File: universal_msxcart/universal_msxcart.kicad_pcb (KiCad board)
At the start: 2 copper layers, 102.5 x 65 mm, 9 parts, among them J1 Conn_01x21_Pin, P1 CONN_02X25, U1 74HC244, U2 74HC244, U3 74HC244, U4 TXB0108PW, U5 74LS08, U6 74LS05, U7 74LS139

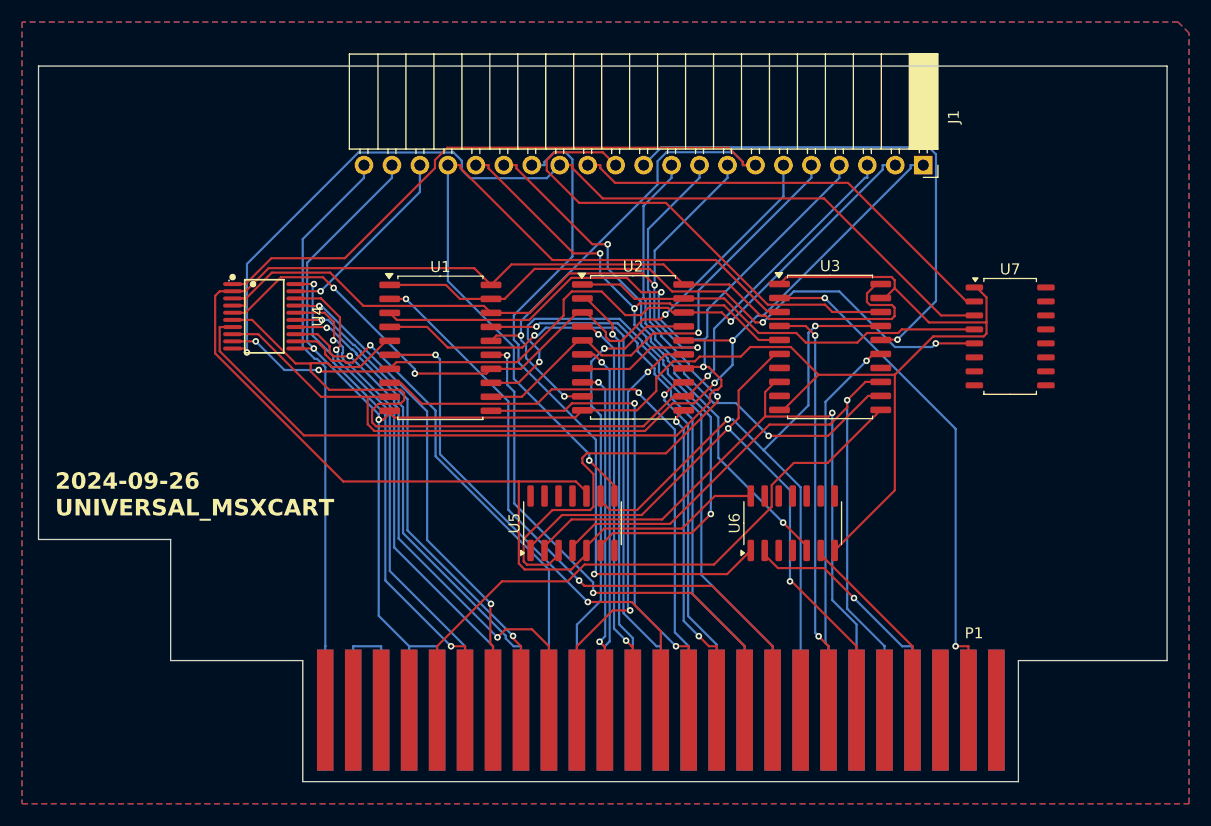
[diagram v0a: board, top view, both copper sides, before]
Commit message: epm240_msxcart/epm240_msxcart.kicad_pcb epm240_msxcart/epm240_msxcart.kicad_prl epm240_msxcart/epm240_msxcart.kicad_sch epm240_msxcart/fp-info-cache epm240_msxcart/freerouting.dsn epm240_msxcart/freerouting.ses universal_msxcart/.gitignore universal_msxcart/fp-info-cache universal_msxcart/universal_msxcart.kicad_pcb universal_msxcart/universal_msxcart.kicad_prl universal_msxcart/universal_msxcart.kicad_sch
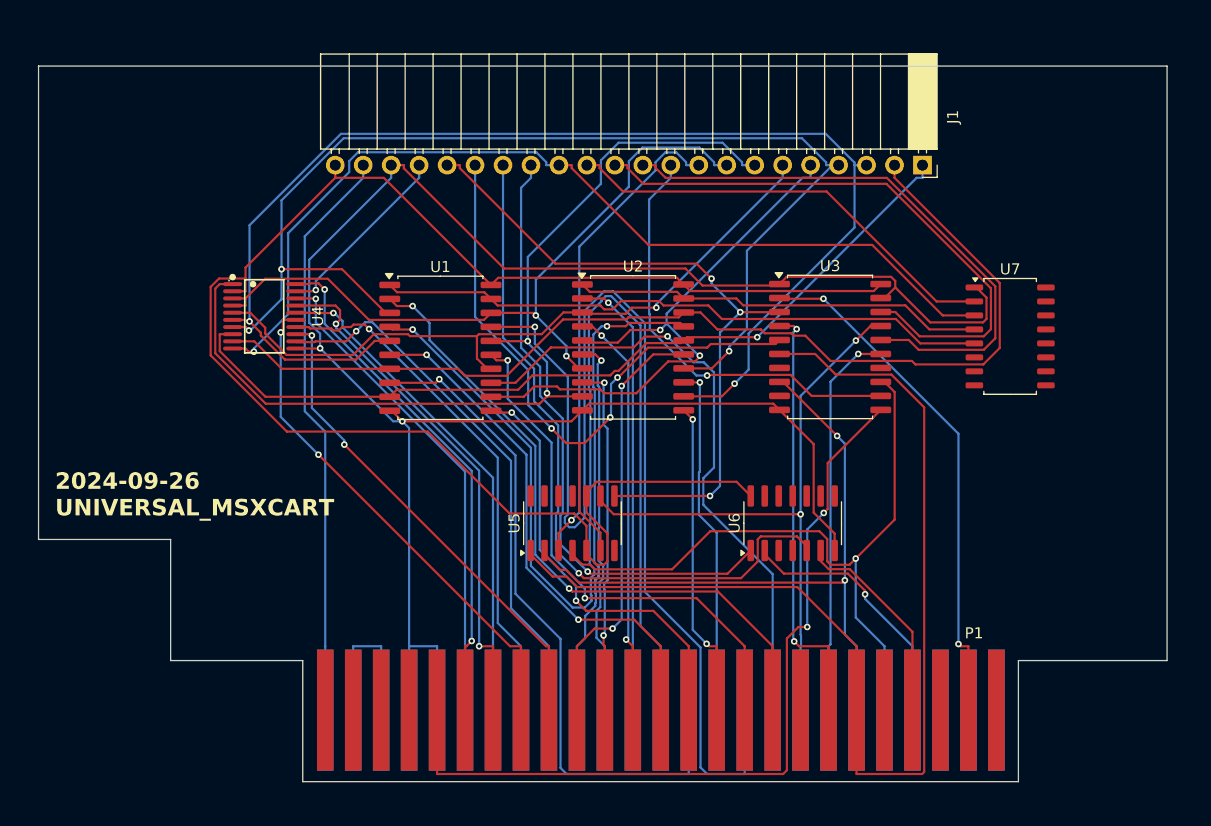
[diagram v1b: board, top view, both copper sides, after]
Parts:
- J1: footprint Connector_PinSocket_2.54mm:PinSocket_1x21_P2.54mm_Horizontal -> Connector_PinSocket_2.54mm:PinSocket_1x22_P2.54mm_Horizontal
- moved J1 0.07 mm to (158.8, 57.0)
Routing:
- net /A11: track 51.6 -> 104.1 mm
- net /A14: track 58.7 -> 104.1 mm
- net /MREQ: track 62.2 -> 99.5 mm, vias 2 -> 0
- net /RD2: track 89.9 -> 115.6 mm, vias 1 -> 2
- net /RD1: track 73.0 -> 96.5 mm, vias 3 -> 0
- net /CLK: track 56.2 -> 74.4 mm, vias 0 -> 2
- net /RC15: track 47.9 -> 64.5 mm, vias 2 -> 1
- net /RC8: track 58.9 -> 43.8 mm
- net /RD4: track 41.9 -> 54.0 mm, vias 1 -> 2
- net /RD7: track 77.6 -> 66.5 mm
- net /RD3: track 116.8 -> 105.9 mm, vias 2 -> 3
- net /RC11: track 43.6 -> 53.9 mm
- net /RC17: track 72.1 -> 62.7 mm, vias 1 -> 3
- net /RD6: track 96.5 -> 87.0 mm
- net /RD0: track 85.8 -> 77.6 mm, vias 2 -> 1
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- removed copper zone on B.Cu, net (none)
- removed copper zone on F.Cu, net (none)

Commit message: universal_msxcart/universal_msxcart.kicad_pcb universal_msxcart/universal_msxcart.kicad_pro universal_msxcart/universal_msxcart.kicad_sch
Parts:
- U1, U2, U3: value 74HC244 -> 74HC245
- U6: value 74LS05 -> 74LS07
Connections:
- P1 pad 45: /5V0 -> +5V
- P1 pad 47: /5V0 -> +5V
- U1 pad 1: /ADDRH -> +3V3
- U1 pad 11: /A8 -> /RD0
- U1 pad 12: /RD4 -> /RD1
- U1 pad 13: /A9 -> /RD2
- U1 pad 14: /RD5 -> /RD3
- U1 pad 15: /A10 -> /RD4
- U1 pad 16: /RD6 -> /RD5
- U1 pad 17: /A11 -> /RD6
- U1 pad 3: /RD3 -> /A14
- U1 pad 4: /A14 -> /A13
- U1 pad 5: /RD2 -> /A12
- U1 pad 6: /A13 -> /A11
- U1 pad 7: /RD1 -> /A10
- U1 pad 8: /A12 -> /A9
- U1 pad 9: /RD0 -> /A8
- U2 pad 1: /ADDRL -> +3V3
- U2 pad 11: /A6 -> /RD6
- U2 pad 12: /RD2 -> /RD7
- U2 pad 13: /A7 -> /RD4
- U2 pad 14: /RD3 -> /RD5
- U2 pad 15: /A4 -> /RD2
- U2 pad 16: /RD0 -> /RD3
- U2 pad 17: /A5 -> /RD0
- U2 pad 3: /RD5 -> /A0
- U2 pad 4: /A0 -> /A3
- U2 pad 5: /RD4 -> /A2
- U2 pad 6: /A3 -> /A5
- U2 pad 7: /RD7 -> /A4
- U2 pad 8: /A2 -> /A7
- U2 pad 9: /RD6 -> /A6
- U3 pad 1: GND -> +3V3
- U3 pad 11: /CLK -> unconnected-(U3-B7-Pad11)
- U3 pad 12: /RC9 -> unconnected-(U3-B6-Pad12)
- U3 pad 13: /M1 -> unconnected-(U3-B5-Pad13)
- U3 pad 15: /WR -> /RC9
- U3 pad 16: /RC10 -> unconnected-(U3-B2-Pad16)
- U3 pad 17: /RESET -> /RC10
- U3 pad 3: /RC17 -> /RD
- U3 pad 4: /RD -> /MREQ
- U3 pad 5: /RC16 -> /IORQ
- U3 pad 6: /MREQ -> /RESET
- U3 pad 7: unconnected-(U3-2Y2-Pad7) -> /WR
- U3 pad 8: /IORQ -> /M1
- U3 pad 9: unconnected-(U3-2Y3-Pad9) -> /CLK
- U7 pad 10: (no net) -> unconnected-(U7B-O2-Pad10)
- U7 pad 11: (no net) -> unconnected-(U7B-O1-Pad11)
- U7 pad 12: (no net) -> unconnected-(U7B-O0-Pad12)
- U7 pad 13: (no net) -> unconnected-(U7B-A1-Pad13)
- U7 pad 14: (no net) -> unconnected-(U7B-A0-Pad14)
- U7 pad 15: (no net) -> unconnected-(U7B-E-Pad15)
- U7 pad 16: (no net) -> +3V3
- U7 pad 8: (no net) -> GND
- U7 pad 9: (no net) -> unconnected-(U7B-O3-Pad9)
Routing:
- net /RD0: track 77.6 -> 136.4 mm
- net +5V: track 17.1 -> 69.0 mm
- net /A11: track 104.1 -> 63.5 mm
- net /A14: track 104.1 -> 63.5 mm
- net /RD3: track 105.9 -> 69.4 mm, vias 3 -> 1
- net /RD7: track 66.5 -> 97.4 mm, vias 2 -> 1
- net /MREQ: track 99.5 -> 73.5 mm
- net /RC10: track 52.6 -> 28.0 mm, vias 0 -> 2
- net GND: track 185.4 -> 208.3 mm
- net /RC11: track 53.9 -> 32.1 mm, vias 0 -> 1
- net /RC17: track 62.7 -> 41.2 mm, vias 3 -> 1
- net /RC16: track 64.2 -> 45.1 mm, vias 3 -> 1
- net /A6: track 28.9 -> 45.0 mm, vias 2 -> 0
- net /RD1: track 96.5 -> 81.7 mm, vias 0 -> 1
- net /RC15: track 64.5 -> 50.0 mm
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- added copper zone on B.Cu, net GND
- added copper zone on F.Cu, net GND

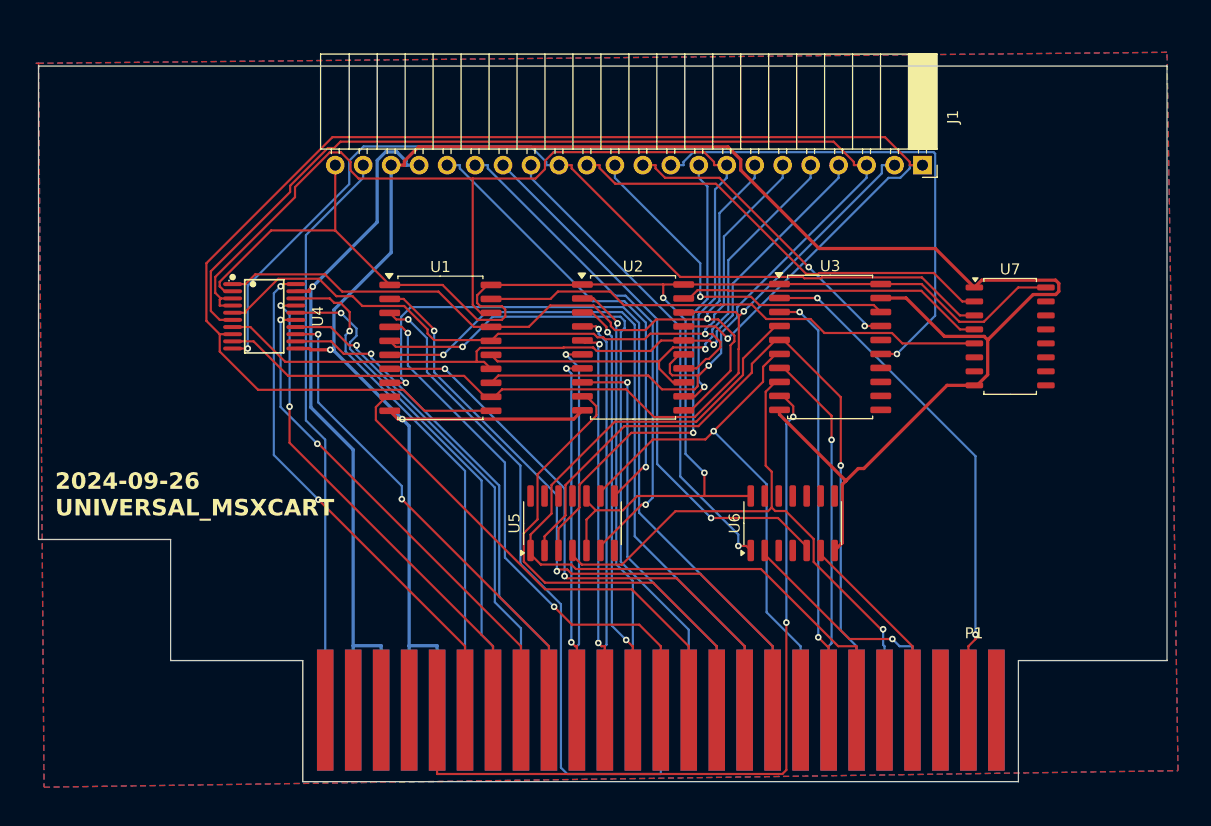
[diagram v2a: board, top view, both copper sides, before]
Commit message: rpmc_epm240/rpmc_epm240.kicad_prl rpmc_logics/rpmc_logics.kicad_pcb rpmc_logics/rpmc_logics.kicad_prl rpmc_logics/rpmc_logics.kicad_sch universal_msxcart/universal_msxcart.kicad_pcb
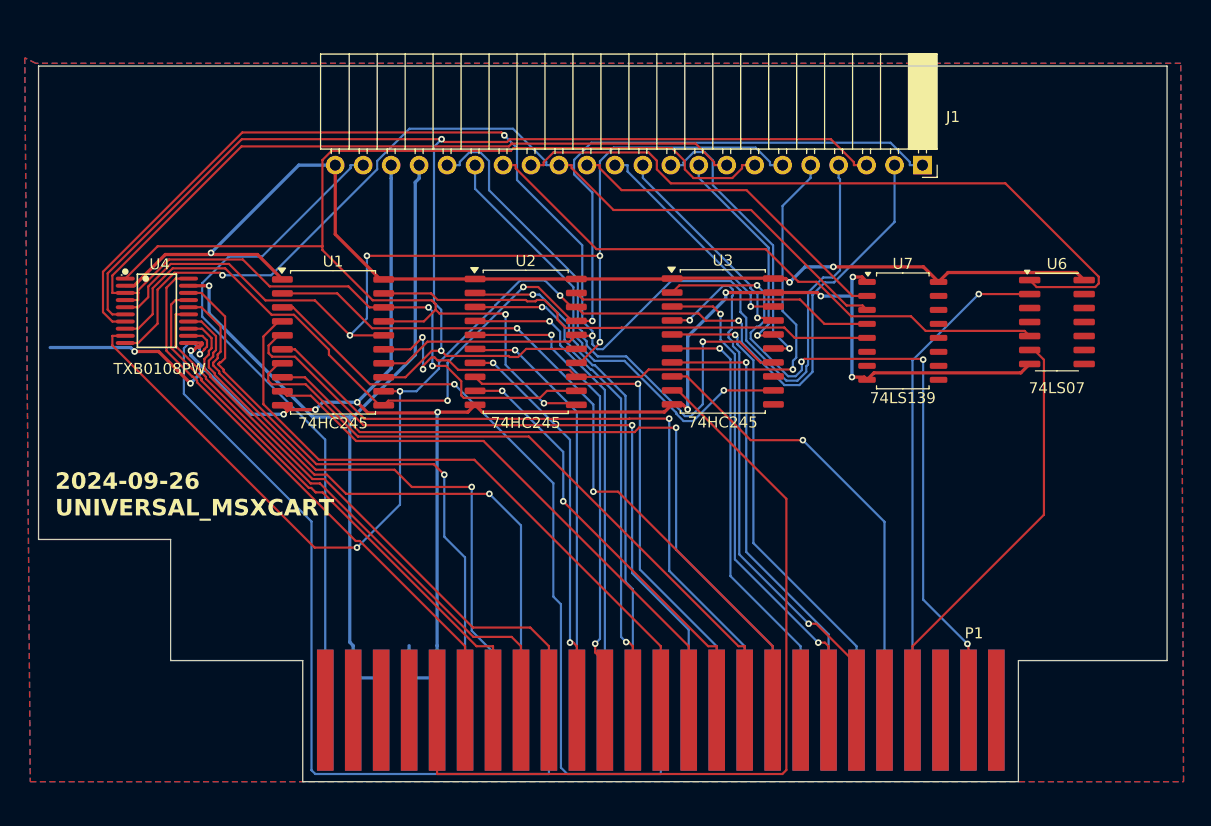
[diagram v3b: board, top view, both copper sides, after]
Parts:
- removed U5: 74LS08, Package_SO:SOIC-14_3.9x8.7mm_P1.27mm
- moved U6 30.2 mm to (171.0, 71.2), turned to 0 degrees
- moved U1 9.76 mm to (105.2, 73.1)
- moved U2 9.76 mm to (122.8, 73.1)
- moved U3 9.76 mm to (140.7, 73.0)
- moved U4 9.76 mm to (89.2, 70.2)
- moved U7 9.76 mm to (157.0, 72.1)
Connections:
- U3 pad 12: unconnected-(U3-B6-Pad12) -> /RC16
- U3 pad 14: unconnected-(U3-B4-Pad14) -> /RC17
- U3 pad 16: unconnected-(U3-B2-Pad16) -> /RC8
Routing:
- net /RD3: track 69.4 -> 139.4 mm, vias 1 -> 2
- net /RD1: track 81.7 -> 119.0 mm, vias 1 -> 4
- net /RD6: track 75.7 -> 106.3 mm, vias 1 -> 2
- net GND: track 208.3 -> 178.2 mm, vias 2 -> 12
- net /D1: track 46.4 -> 76.3 mm
- net +3V3: track 139.0 -> 109.1 mm, vias 2 -> 3
- net /RD0: track 136.4 -> 107.9 mm, vias 1 -> 3
- net /IORQ: track 68.8 -> 44.4 mm
- net /RC8: track 44.2 -> 20.0 mm
- net /MREQ: track 73.5 -> 50.6 mm, vias 0 -> 2
- net /RD5: track 72.1 -> 94.7 mm, vias 1 -> 4
- net /WAIT: track 23.0 -> 44.9 mm
- net /RC14: track 43.7 -> 64.6 mm, vias 1 -> 0
- net /INT: track 18.0 -> 38.4 mm
- net /RD7: track 97.4 -> 117.8 mm, vias 1 -> 2
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
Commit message: ../universal_msxcart/universal_msxcart.kicad_pcb ../universal_msxcart/universal_msxcart.kicad_prl
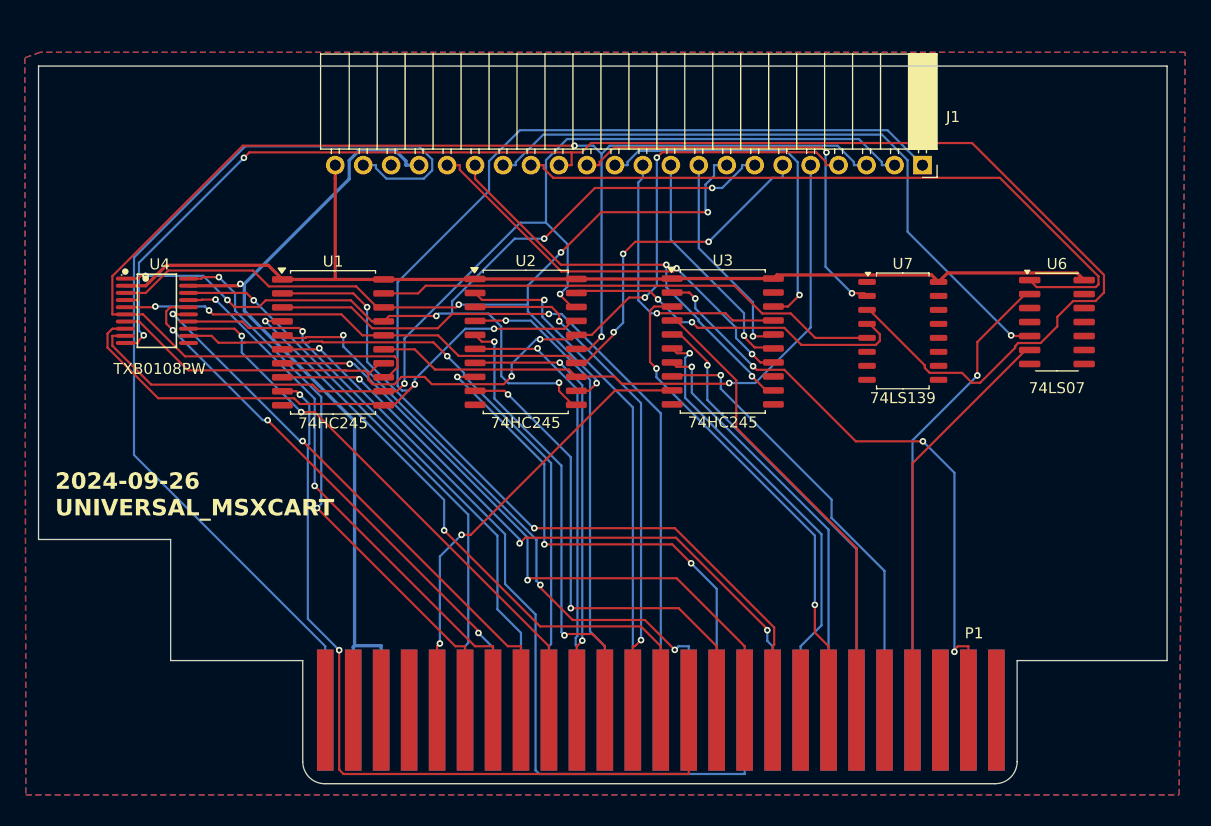
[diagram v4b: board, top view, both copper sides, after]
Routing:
- net GND: track 178.2 -> 0.00 mm, vias 12 -> 0
- net /RC13: track 85.0 -> 138.3 mm, vias 1 -> 2
- net /RD3: track 139.4 -> 86.7 mm, vias 2 -> 4
- net /RD7: track 117.8 -> 79.2 mm, vias 2 -> 4
- net /CLK: track 76.8 -> 41.4 mm, vias 0 -> 2
- net /SOUNDIN: track 62.6 -> 88.3 mm
- net /A8: track 52.3 -> 75.1 mm, vias 0 -> 2
- net /RD6: track 106.3 -> 84.0 mm, vias 2 -> 6
- net /RD5: track 94.7 -> 73.8 mm, vias 4 -> 5
- net /RD1: track 119.0 -> 100.8 mm, vias 4 -> 2
- net /D1: track 76.3 -> 60.5 mm
- net /RC17: track 51.8 -> 38.1 mm, vias 1 -> 2
- net /RC11: track 20.7 -> 32.7 mm
- net /RD0: track 107.9 -> 119.0 mm, vias 3 -> 2
- net +3V3: track 109.1 -> 99.8 mm, vias 3 -> 0
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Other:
- board size 102.5 x 65 mm -> 102.5 x 65.2 mm
